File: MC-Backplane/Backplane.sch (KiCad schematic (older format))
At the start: 1 part

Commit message: Add files via upload
updating net names and wires
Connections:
- net GND: now reaches J?.2
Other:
- note added: "Slots 1-3"
- note added: "slot 10-13"
- note added: "slot 7&8"
- note added: "slot 9"
- note added: "slots 4-6"
- note removed: "Global reset to/from all cards and DSP\nFO enable b/w DSP and FO card only"
- moved on the sheet: J?

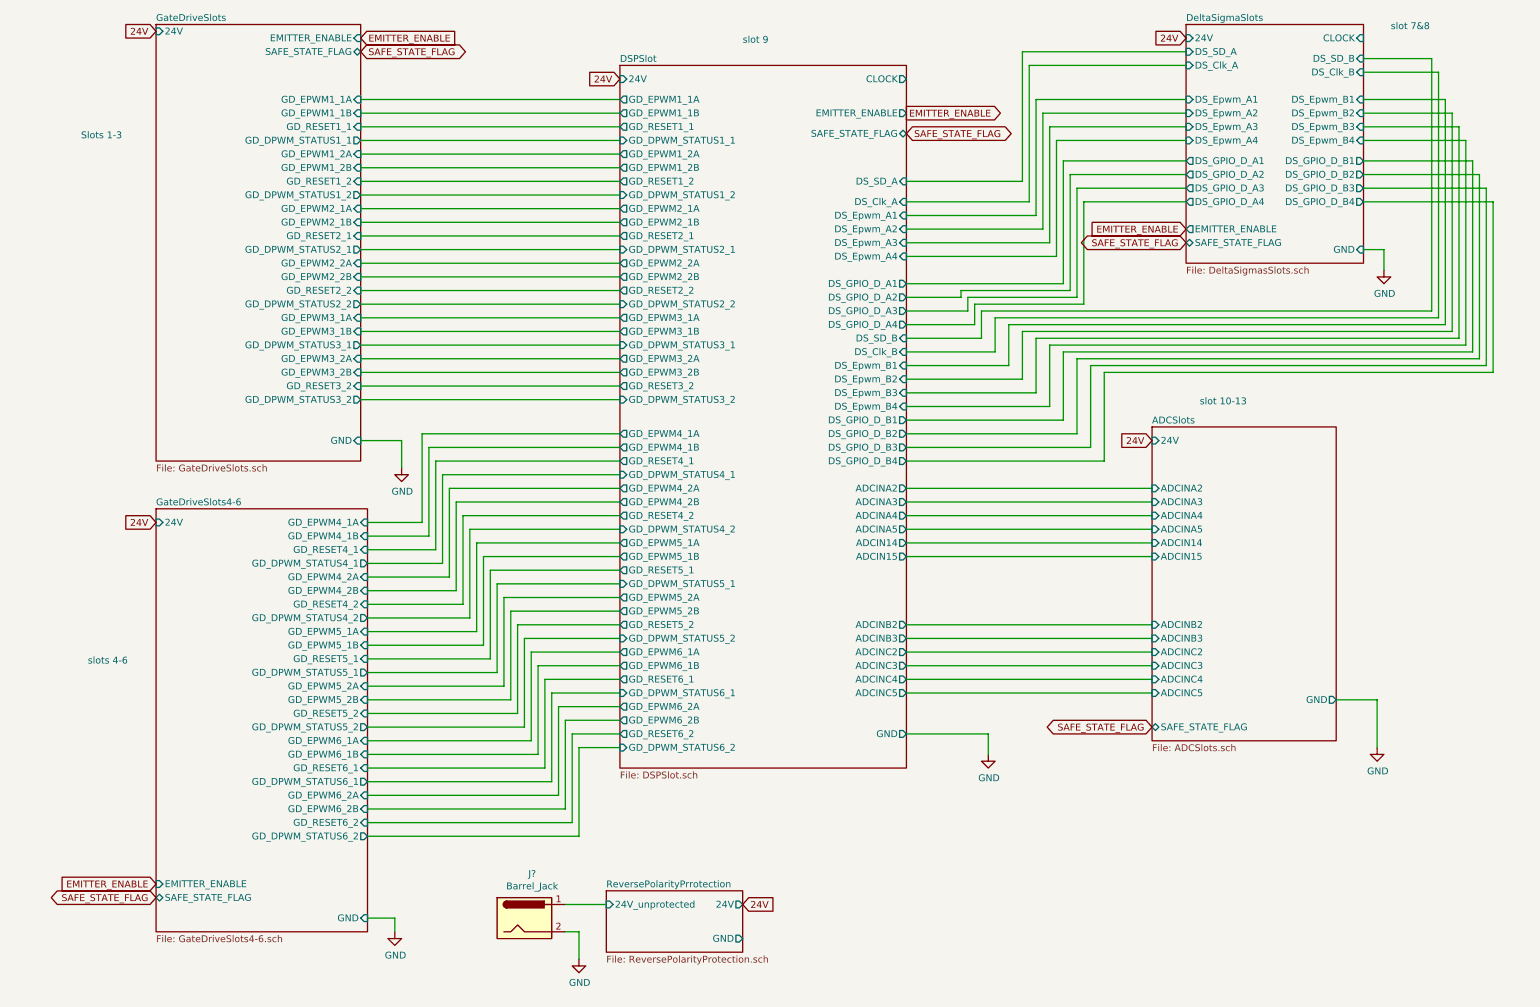
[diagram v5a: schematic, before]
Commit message: Signal naming cleanup/ dsp pin pairing
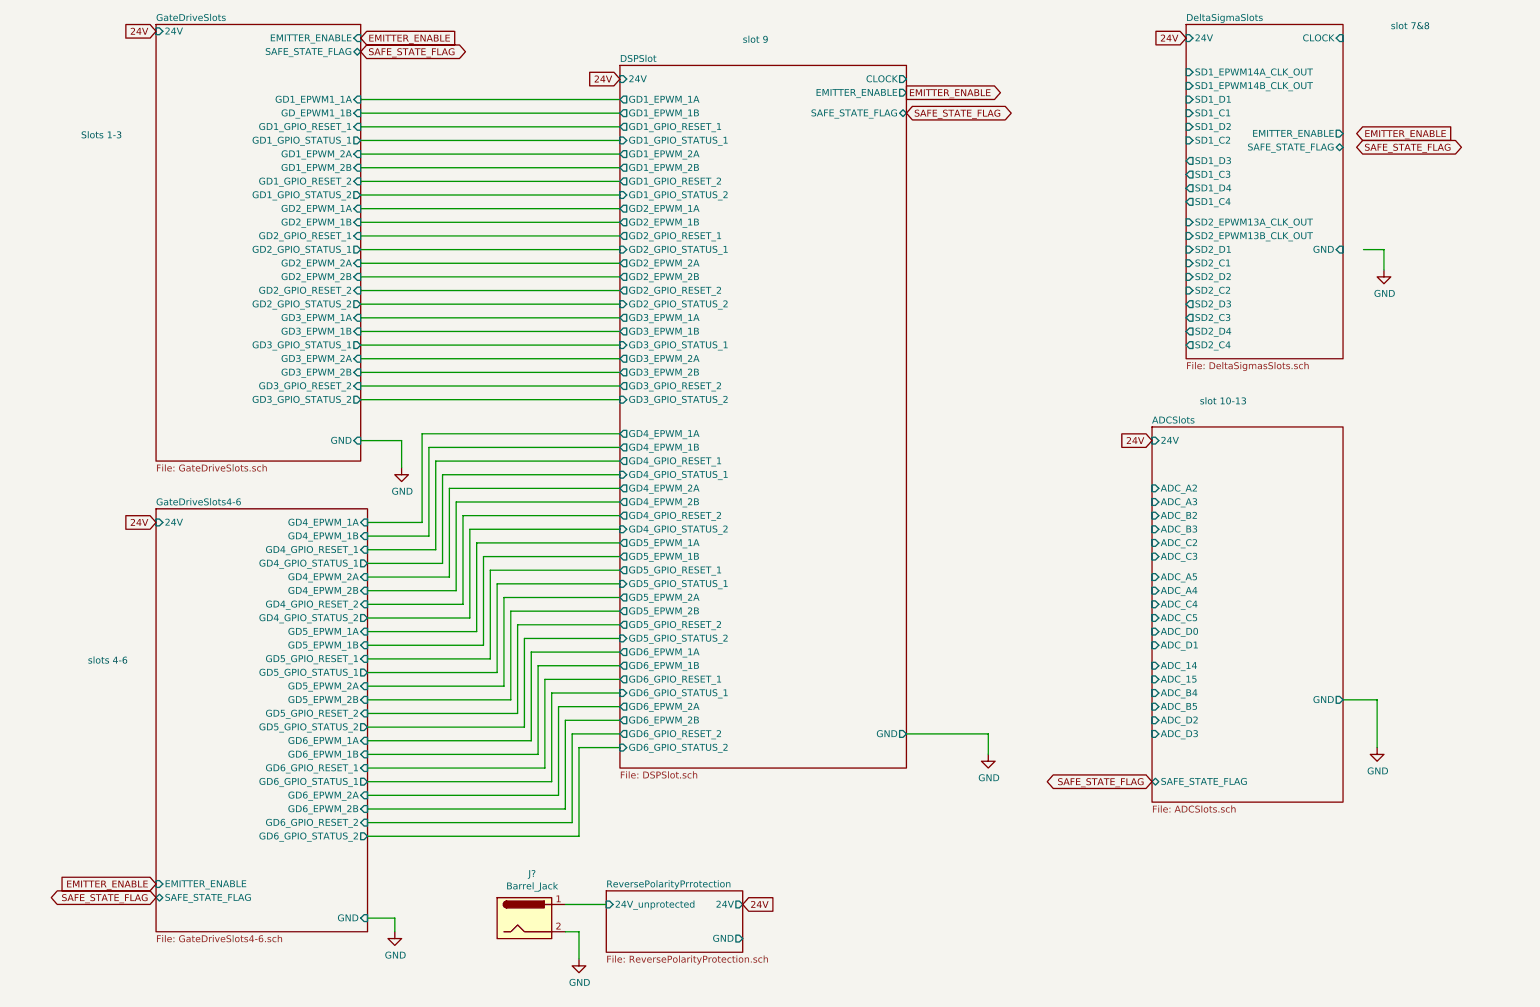
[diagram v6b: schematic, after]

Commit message: Prep for DSP connector
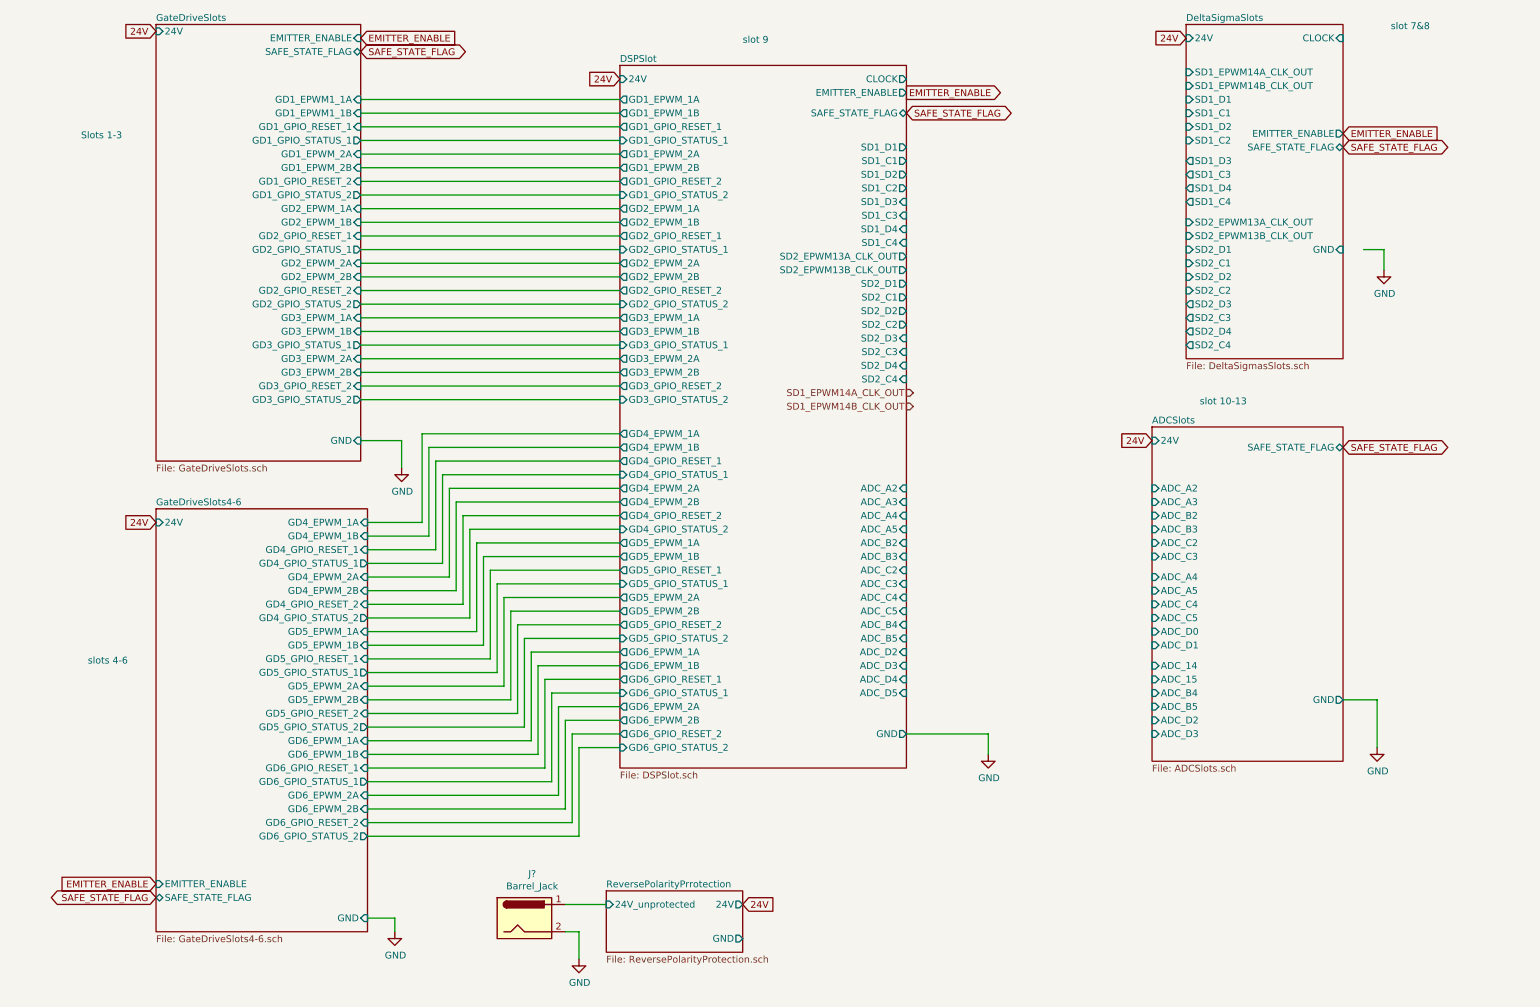
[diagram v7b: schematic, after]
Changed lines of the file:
@@
 F3 "GND" I R 2750 3650 50
 F4 "GD1_EPWM1_1A" I R 2750 1150 50
-F5 "GD_EPWM1_1B" I R 2750 1250 50
+F5 "GD1_EPWM1_1B" I R 2750 1250 50
 F6 "GD1_GPIO_RESET_1" I R 2750 1350 50
 F7 "GD1_GPIO_STATUS_1" O R 2750 1450 50
@@
 Text GLabel 6750 1250 2    50   BiDi ~ 0
 SAFE_STATE_FLAG
-Text GLabel 8550 6150 0    50   BiDi ~ 0
+Text GLabel 9950 3700 2    50   BiDi ~ 0
 SAFE_STATE_FLAG
 Text GLabel 6750 1100 2    50   Output ~ 0
 EMITTER_ENABLE
-Text GLabel 10050 1400 2    50   Input ~ 0
+Text GLabel 9950 1400 2    50   Input ~ 0
 EMITTER_ENABLE
-Text GLabel 10050 1500 2    50   BiDi ~ 0
+Text GLabel 9950 1500 2    50   BiDi ~ 0
 SAFE_STATE_FLAG
 $Comp
@@
 F52 "SAFE_STATE_FLAG" B R 6750 1250 50
 F53 "GND" O R 6750 5800 50
+F54 "SD1_D1" O R 6750 1500 50
+F55 "SD1_C1" O R 6750 1600 50
+F56 "SD1_D2" O R 6750 1700 50
+F57 "SD1_C2" O R 6750 1800 50
+F58 "SD1_D3" I R 6750 1900 50
+F59 "SD1_C3" I R 6750 2000 50
+F60 "SD1_D4" I R 6750 2100 50
+F61 "SD1_C4" I R 6750 2200 50
+F62 "SD2_D1" O R 6750 2500 50
+F63 "SD2_C1" O R 6750 2600 50
+F64 "SD2_D2" O R 6750 2700 50
+F65 "SD2_C2" O R 6750 2800 50
+F66 "SD2_D3" I R 6750 2900 50
+F67 "SD2_C3" I R 6750 3000 50
+F68 "SD2_D4" I R 6750 3100 50
+F69 "SD2_C4" I R 6750 3200 50
+F70 "ADC_A2" I R 6750 4000 50
+F71 "ADC_A3" I R 6750 4100 50
+F72 "ADC_A4" I R 6750 4200 50
+F73 "ADC_A5" I R 6750 4300 50
+F74 "ADC_B2" I R 6750 4400 50
+F75 "ADC_B3" I R 6750 4500 50
+F76 "ADC_C2" I R 6750 4600 50
+F77 "ADC_C3" I R 6750 4700 50
+F78 "ADC_C4" I R 6750 4800 50
+F79 "ADC_C5" I R 6750 4900 50
+F80 "ADC_B4" I R 6750 5000 50
+F81 "ADC_B5" I R 6750 5100 50
+F82 "ADC_D2" I R 6750 5200 50
+F83 "ADC_D3" I R 6750 5300 50
+F84 "ADC_D4" I R 6750 5400 50
+F85 "ADC_D5" I R 6750 5500 50
+F86 "SD2_EPWM13A_CLK_OUT" O R 6750 2300 50
+F87 "SD2_EPWM13B_CLK_OUT" O R 6750 2400 50
 $EndSheet
 $Sheet
-S 8550 3550 1400 2750
+S 8550 3550 1400 2450
 U 61E8CB26
 F0 "ADCSlots" 50
 F1 "ADCSlots.sch" 50
 F2 "24V" I L 8550 3650 50
-F3 "SAFE_STATE_FLAG" B L 8550 6150 50
+F3 "SAFE_STATE_FLAG" B R 9950 3700 50
 F4 "GND" O R 9950 5550 50
 F5 "ADC_A2" I L 8550 4000 50
 F6 "ADC_A3" I L 8550 4100 50
-F7 "ADC_A4" I L 8550 4750 50
-F8 "ADC_A5" I L 8550 4650 50
+F7 "ADC_A4" I L 8550 4650 50
+F8 "ADC_A5" I L 8550 4750 50
 F9 "ADC_B2" I L 8550 4200 50
 F10 "ADC_B3" I L 8550 4300 50
@@
 F22 "ADC_D1" I L 8550 5150 50
 $EndSheet
+Text HLabel 6800 3300 0    50   Input ~ 0
+SD1_EPWM14A_CLK_OUT
+Text HLabel 6800 3400 0    50   Input ~ 0
+SD1_EPWM14B_CLK_OUT
 $EndSCHEMATC
